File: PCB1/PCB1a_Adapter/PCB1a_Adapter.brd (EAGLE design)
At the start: 125.6 x 84.2 mm, 28 parts, among them J1 691357310006B, J2 618009231421, J5 61004021821, J6 61004021821, U2 MAX232D, U4 TLE9250VSJ, U8 74AHCT245, U9 74AHCT245

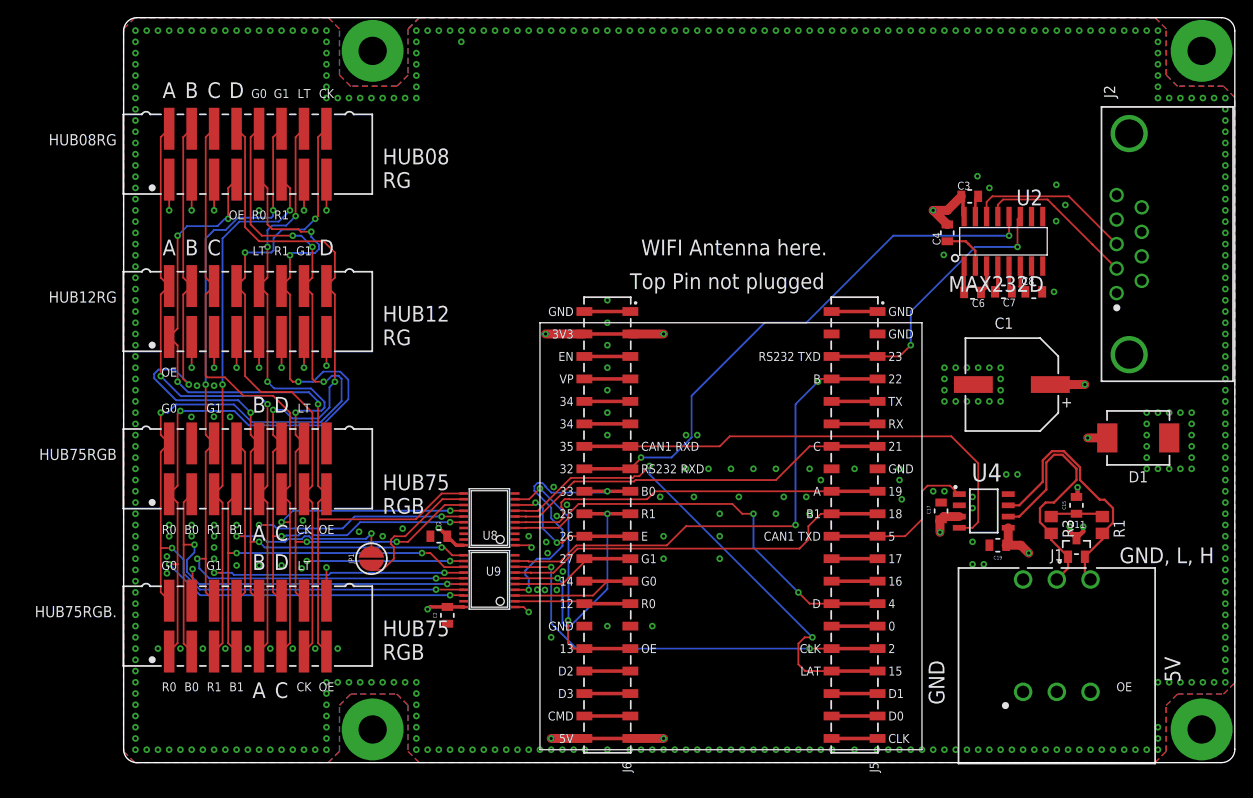
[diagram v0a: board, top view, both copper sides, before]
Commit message: Update PCB design settings and connector library description.
- Update PCB design settings for vector font to "alwaysvectorfont=yes" and vertical text to "up".
- Remove specific library references from the PCB design file.
- Modify a connector library description in the board file.
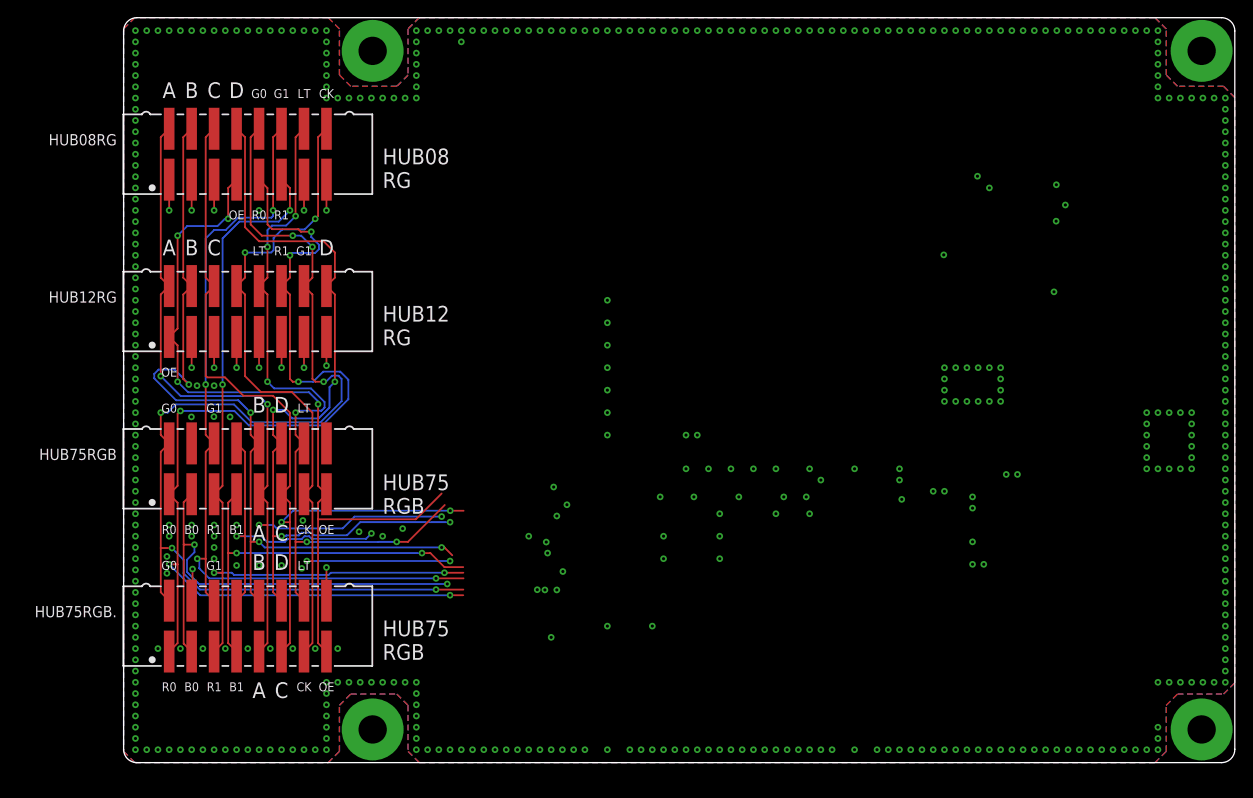
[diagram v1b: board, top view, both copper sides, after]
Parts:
- removed C1: 470uF, Wurth_Capacitors_WCAP-AS5H:WCAP-AS5H_10X10.5(DXL)
- removed C15: 47nF, Wurth_Capacitors_WCAP-CSGP:WCAP-CSGP_0805_H0.8_R
- removed C17, C19, C2, C3, C4, C5, C6, C7, C8: 100nF, Wurth_Capacitors_WCAP-CSGP:WCAP-CSGP_0805_H0.8_R
- removed D1: 5V, Wurth_EMC Components_WE-TVSP:WE-TVSP_DO-214AB_BIDIRECTIONAL
- removed D11: 24Vdc, Wurth_EMC Components_WE-TVS:WE-TVS_SOT23-3L
- removed J1: 691357310006B, Wurth_Connectors_WR-TBL Pluggable Connector:691357310006B
- removed J2: 618009231421, Wurth_Connectors_WR-DSUB:618009231421
- removed J5, J6: 61004021821, Wurth_Connectors_WR-PHD:61004021821
- removed JP1: JUMPER-SMT_2_NO_SILK_ROUND, SparkFun-Jumpers:SMT-JUMPER_2_NO_SILK_ROUND
- removed R1, R3: 60R, resistor:R0805
- removed U2: MAX232D, IC:SOIC16
- removed U4: TLE9250VSJ, TLE9250VSJ:SOIC127P602X173-8N-V
- removed U8, U9: 74AHCT245, microbuilder:TSSOP20
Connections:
- removed net +3V3: C19.1, C3.1, C4.2, J6.3, J6.4, U2.16, U4.5
- removed net +5V: C1.1, C17.1, C2.2, C5.2, D1.2, J1.3, J6.39, J6.40, U4.3, U8.1, U8.20, U9.1, U9.20
- removed net 0: J5.29, J5.30
- removed net 16: J5.25, J5.26
- removed net 17: J5.23, J5.24
- removed net 232_RX: J2.2, U2.13
- removed net 232_TX: J2.3, U2.14
- removed net 34: J6.11, J6.12
- removed net ADDRA_3V: J5.17, J5.18, U8.5
- removed net ADDRB_3V: J5.7, J5.8, U9.9
- removed net ADDRC_3V: J5.13, J5.14, U8.6
- removed net ADDRD_3V: J5.27, J5.28, U8.4
- removed net ADDRE_3V: J6.21, J6.22, U8.8
- removed net B0_3V: J6.17, J6.18, U9.4
- removed net B1_3V: J5.19, J5.20, U9.7
- removed net CAN1_RXD: J6.13, J6.14, U4.4
- removed net CAN1_TXD: J5.21, J5.22, U4.1
- removed net CAN_N: D11.1, J1.5, R3.2, U4.6
- removed net CAN_P: D11.2, J1.6, R1.2, U4.7
- removed net CLK: J5.39, J5.40
- removed net CLK_3V: J5.31, J5.32, U9.8
- removed net CMD: J6.37, J6.38
- removed net D0: J5.37, J5.38
- removed net D1: J5.35, J5.36
- removed net D2: J6.33, J6.34
- removed net D3: J6.35, J6.36
- removed net EN: J6.5, J6.6
- removed net G0_3V: J6.25, J6.26, U9.3
- removed net G1_3V: J6.23, J6.24, U9.5
- removed net LAT_3V: J5.33, J5.34, U8.7
- removed net M1_E_NC: JP1.1, U8.12
- removed net N$20: C15.1, R1.1, R3.1
- removed net N$33: C6.2, U2.1
- removed net N$34: C6.1, U2.3
- removed net N$35: C7.2, U2.4
- removed net N$36: C7.1, U2.5
- removed net N$37: C4.1, U2.2
- removed net N$38: C8.1, U2.6
- removed net N$39: U2.9
- removed net N$40: U2.10
- removed net N$46: U2.7
- removed net N$47: U2.8
- removed net OE_3V: J6.31, J6.32, U8.9
- removed net R0_3V: J6.27, J6.28, U9.2
- removed net R1_3V: J6.19, J6.20, U9.6
- removed net RX: J6.15, J6.16, U2.12
- removed net TX: J5.5, J5.6, U2.11
- removed net USB_RX: J5.11, J5.12
- removed net USB_TX: J5.10, J5.9
- removed net VN: J6.10, J6.9
- removed net VP: J6.7, J6.8
- net GND: no longer C1.2, C15.2, C17.2, C19.2, C2.1, C3.2, C5.1, C8.2, D1.1, D11.3, J1.1, J1.4, J2.5, J2.S1, J2.S2, J5.1, J5.15, J5.16, J5.2, J5.3, J5.4, J6.1, J6.2, J6.29, J6.30, U2.15, U4.2, U4.8, U8.10, U8.19, U8.2, U8.3, U9.10, U9.19
- net M1_A: no longer U8.15
- net M1_B: no longer U9.11
- net M1_B0: no longer U9.16
- net M1_B1: no longer U9.13
- net M1_C: no longer U8.14
- net M1_CLK: no longer U9.12
- net M1_D: no longer U8.16
- net M1_E: no longer JP1.2
- net M1_G0: no longer U9.17
- net M1_G1: no longer U9.15
- net M1_LAT: no longer U8.13
- net M1_OE: no longer U8.11
- net M1_R0: no longer U9.18
- net M1_R1: no longer U9.14
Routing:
- net +3V3: track 138.2 -> 0.00 mm, vias 4 -> 0
- net RX: track 63.9 -> 0.00 mm, vias 2 -> 0
- net LAT_3V: track 57.8 -> 0.00 mm, vias 2 -> 0
- net ADDRB_3V: track 57.5 -> 0.00 mm, vias 2 -> 0
- net CAN1_RXD: track 55.3 -> 0.00 mm
- net ADDRD_3V: track 49.2 -> 0.00 mm, vias 2 -> 0
- net CLK_3V: track 48.5 -> 0.00 mm, vias 2 -> 0
- net B1_3V: track 44.6 -> 0.00 mm
- net ADDRC_3V: track 44.2 -> 0.00 mm
- net ADDRA_3V: track 43.8 -> 0.00 mm
- net +5V: track 34.0 -> 0.00 mm, vias 9 -> 0
- net TX: track 31.9 -> 0.00 mm, vias 2 -> 0
- net B0_3V: track 31.5 -> 0.00 mm, vias 2 -> 0
- net R1_3V: track 30.8 -> 0.00 mm, vias 2 -> 0
- net CAN_N: track 29.7 -> 0.00 mm
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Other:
- board text removed: "+5V"
- board text removed: "0"
- board text removed: "1"
- board text removed: "12"
- board text removed: "13"
- board text removed: "14"
- board text removed: "15"
- board text removed: "16"
- board text removed: "17"
- board text removed: "18"
- board text removed: "19"
- board text removed: "2"
- board text removed: "21"
- board text removed: "22"
- board text removed: "23"
- board text removed: "25"
- board text removed: "26"
- board text removed: "27"
- board text removed: "32"
- board text removed: "33"
- board text removed: "34"
- board text removed: "35"
- board text removed: "3V3"
- board text removed: "4"
- board text removed: "5"
- board text removed: "5V"
- board text removed: "6"
- board text removed: "9"
- board text removed: "CAN1 RXD"
- board text removed: "CAN1 TXD"
- board text removed: "CLK"
- board text removed: "CMD"
- board text removed: "D0"
- board text removed: "D1"
- board text removed: "D2"
- board text removed: "D3"
- board text removed: "E"
- board text removed: "EN"
- board text removed: "GND"
- board text removed: "GND, L, H"
- board text removed: "H"
- board text removed: "L"
- board text removed: "LAT"
- board text removed: "RS232 RXD"
- board text removed: "RS232 TXD"
- board text removed: "RX"
- board text removed: "TX"
- board text removed: "Top Pin not plugged"
- board text removed: "VP"
- board text removed: "WIFI Antenna here."
